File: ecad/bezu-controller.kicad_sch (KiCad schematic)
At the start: 0 parts

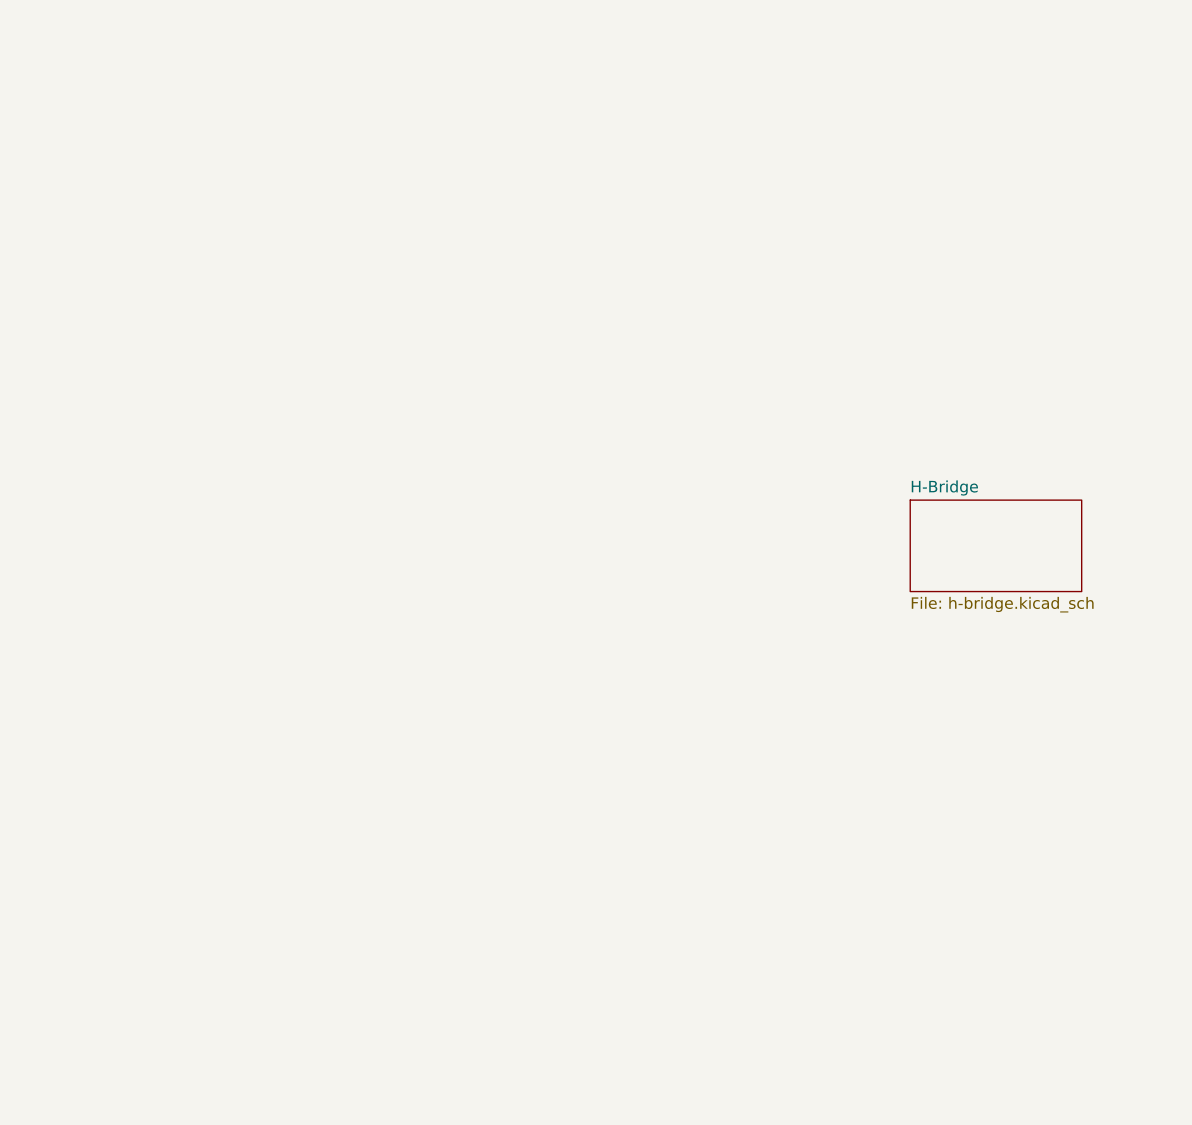
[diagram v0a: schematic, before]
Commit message: Initial half bridge layout
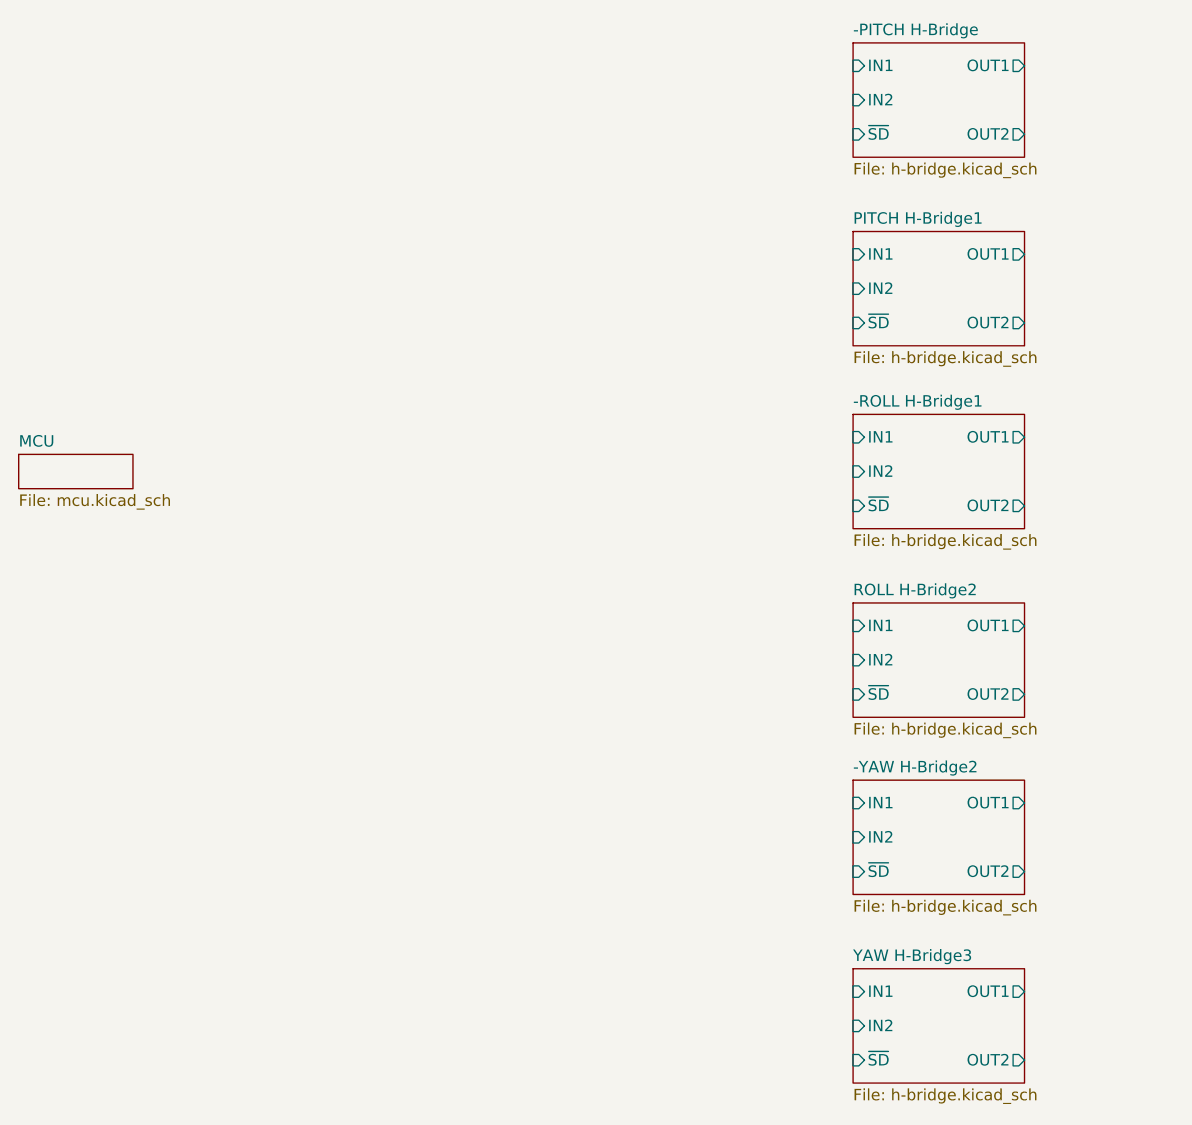
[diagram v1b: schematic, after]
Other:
- sheet H-Bridge renamed -PITCH H-Bridge
- added sheet -ROLL H-Bridge1 (h-bridge.kicad_sch)
- added sheet -YAW H-Bridge2 (h-bridge.kicad_sch)
- added sheet MCU (mcu.kicad_sch)
- added sheet PITCH H-Bridge1 (h-bridge.kicad_sch)
- added sheet ROLL H-Bridge2 (h-bridge.kicad_sch)
- added sheet YAW H-Bridge3 (h-bridge.kicad_sch)
- sheet -PITCH H-Bridge ports: added IN1, IN2, OUT1, OUT2, ~{SD}; removed none

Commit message: Remove numbers frmo sheet instances
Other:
- sheet -ROLL H-Bridge1 renamed -ROLL H-Bridge
- sheet -YAW H-Bridge2 renamed -YAW H-Bridge
- sheet PITCH H-Bridge1 renamed PITCH H-Bridge
- sheet ROLL H-Bridge2 renamed ROLL H-Bridge
- sheet YAW H-Bridge3 renamed YAW H-Bridge
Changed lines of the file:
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@@
 			(color 0 0 0 0.0000)
 		)
-		(property "Sheetname" "-ROLL H-Bridge1"
+		(property "Sheetname" "-ROLL H-Bridge"
 			(at 134.62 86.2834 0)
 			(effects
@@
 			(color 0 0 0 0.0000)
 		)
-		(property "Sheetname" "ROLL H-Bridge2"
+		(property "Sheetname" "ROLL H-Bridge"
 			(at 134.62 107.2384 0)
 			(effects
@@
 			(color 0 0 0 0.0000)
 		)
-		(property "Sheetname" "YAW H-Bridge3"
+		(property "Sheetname" "YAW H-Bridge"
 			(at 134.62 147.8784 0)
 			(effects
@@
 			(color 0 0 0 0.0000)
 		)
-		(property "Sheetname" "-YAW H-Bridge2"
+		(property "Sheetname" "-YAW H-Bridge"
 			(at 134.62 126.9234 0)
 			(effects
@@
 			(color 0 0 0 0.0000)
 		)
-		(property "Sheetname" "PITCH H-Bridge1"
+		(property "Sheetname" "PITCH H-Bridge"
 			(at 134.62 65.9634 0)
 			(effects
